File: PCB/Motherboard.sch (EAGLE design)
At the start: 30 parts, among them IC1 7805TV, IC2 NE555, Q1 BS250

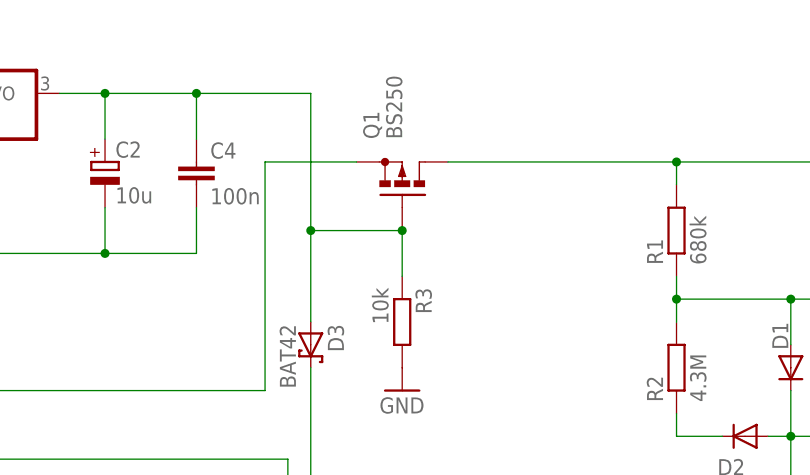
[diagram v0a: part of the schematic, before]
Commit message: Renamed some signals
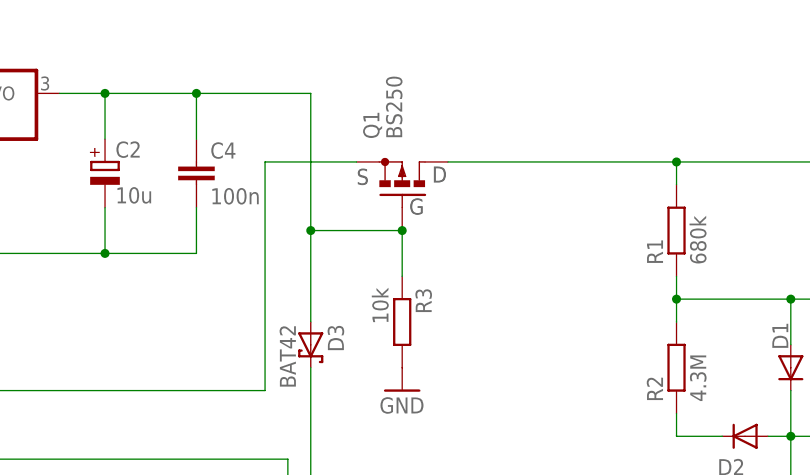
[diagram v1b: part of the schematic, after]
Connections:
- net N$22 renamed A0
- net N$23 renamed A1
- net N$24 renamed A2
- net N$25 renamed A3
- net N$4 renamed S
- net N$5 renamed G
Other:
- note added: "D"
- note added: "G"
- note added: "S"
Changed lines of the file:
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@@
 <sheet>
 <plain>
+<text x="38.1" y="73.66" size="1.778" layer="97">S</text>
+<text x="43.942" y="70.358" size="1.778" layer="97">G</text>
+<text x="46.482" y="73.914" size="1.778" layer="97">D</text>
 </plain>
 <instances>
@@
 </segment>
 </net>
-<net name="N$4" class="0">
+<net name="S" class="0">
 <segment>
 <pinref part="9V" gate="K" pin="K1"/>
@@
 </segment>
 </net>
-<net name="N$5" class="0">
+<net name="G" class="0">
 <segment>
 <pinref part="IC1" gate="A1" pin="VO"/>
@@
 </segment>
 </net>
-<net name="N$22" class="0">
+<net name="A0" class="0">
 <segment>
 <pinref part="ARDUINO_NANO1" gate="G$1" pin="ADC0/A0"/>
@@
 </segment>
 </net>
-<net name="N$23" class="0">
+<net name="A1" class="0">
 <segment>
 <pinref part="ARDUINO_NANO1" gate="G$1" pin="ADC1/A1"/>
@@
 </segment>
 </net>
-<net name="N$24" class="0">
+<net name="A2" class="0">
 <segment>
 <pinref part="ARDUINO_NANO1" gate="G$1" pin="ADC2/A2"/>
@@
 </segment>
 </net>
-<net name="N$25" class="0">
+<net name="A3" class="0">
 <segment>
 <pinref part="ARDUINO_NANO1" gate="G$1" pin="ADC3/A3"/>
